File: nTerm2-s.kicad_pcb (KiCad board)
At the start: 2 copper layers, 147.3 x 55.9 mm, 108 parts, among them J1 VGA, J2 Keyboard, J3 Mouse, J4 Line-out/Speaker, J5 RS-232 V.24, J6 USB_C_Receptacle_USB2.0_16P, J7 Line-out/Speaker, K1 IM41 3V, K2 IM41 3V, K3 IM41 3V, Q1 BC817, Q2 BC817, Q3 BC817, Q4 BC817, Q5 BC817, Q6 BC817, Q7 BC817, Q8 BC817, SW1 IO0, SW2 RESET, SW3 DEFAULTS, U1 ESP32-WROOM-32, U2 LM386, U3 MAX3232E, U4 CP2102N-Axx-xQFN28, U5 NCP1117-3.3_SOT223, U6 USBLC6-2SC6

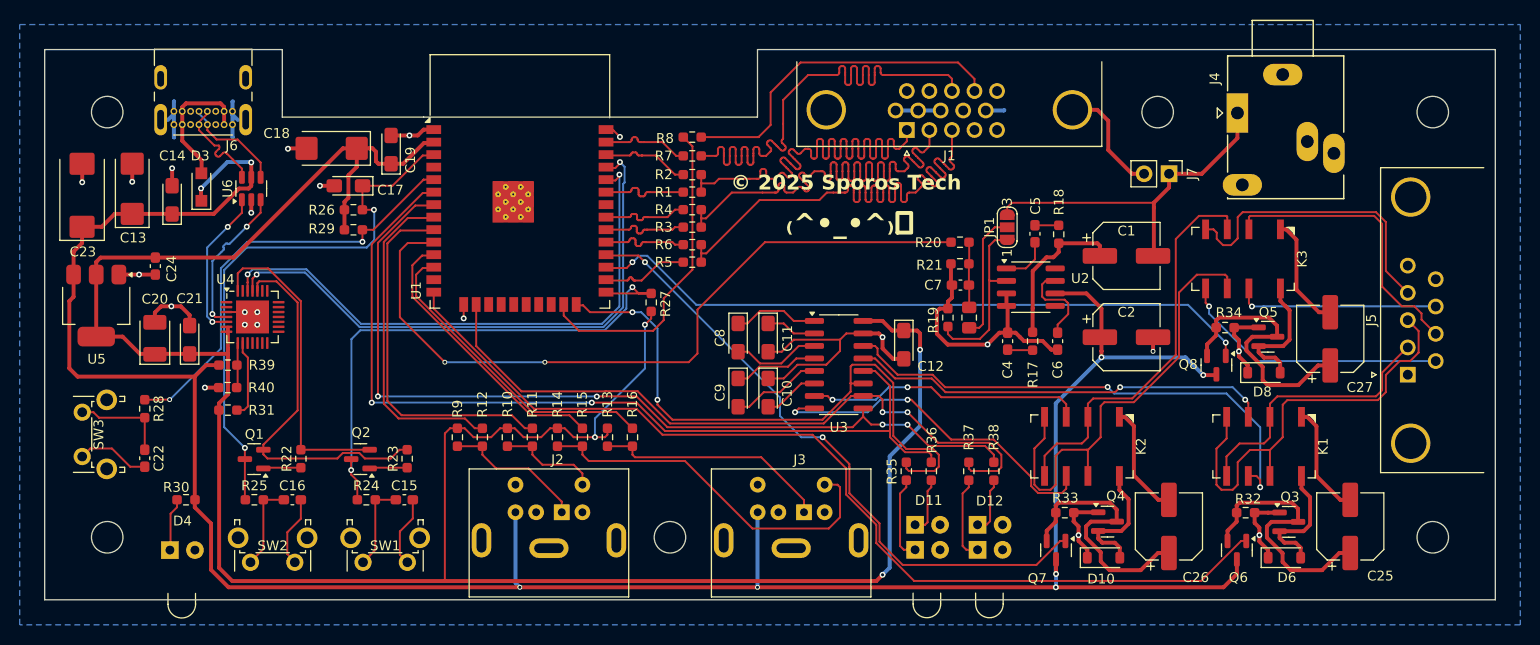
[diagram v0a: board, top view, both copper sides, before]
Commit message: Some small updates, a fix, and exported all libraries into the project, for distribution.
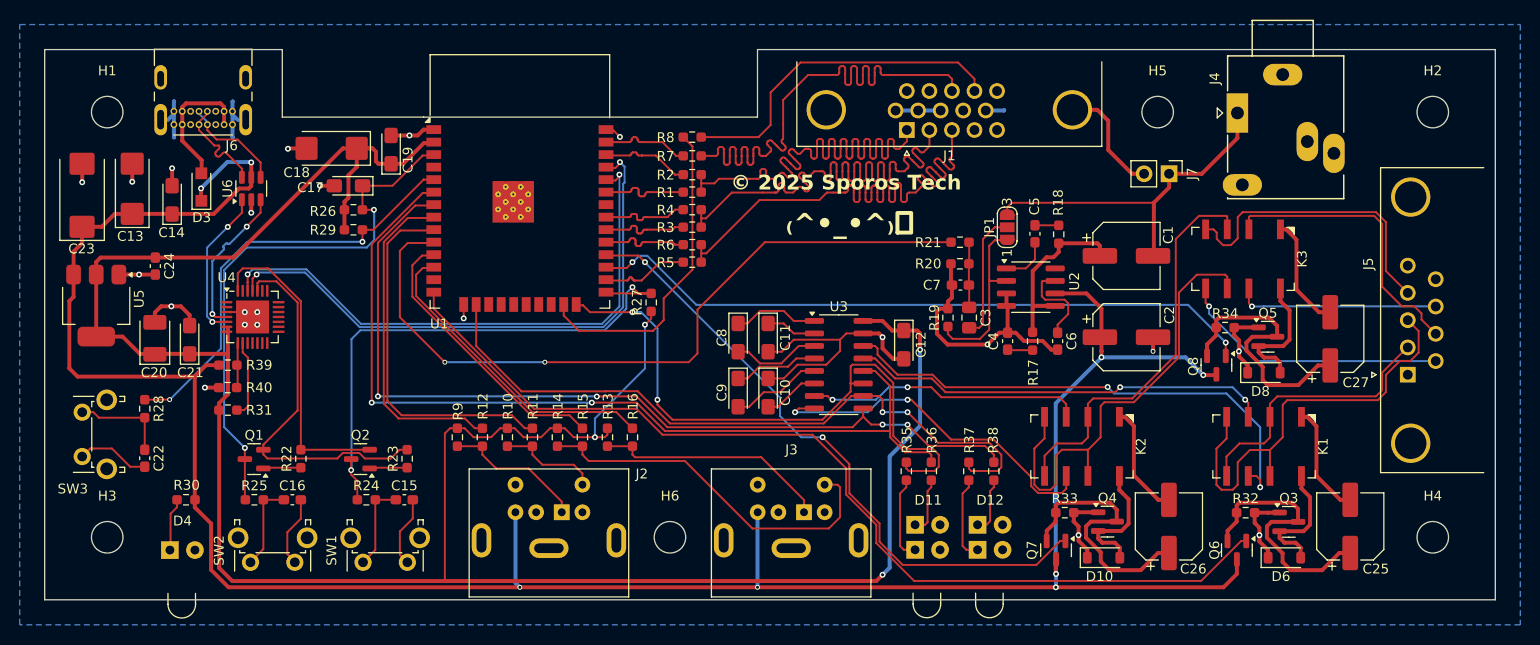
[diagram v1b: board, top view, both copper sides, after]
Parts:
- C1, C2, C25, C26, C27: footprint Capacitor_SMD:CP_Elec_6.3x7.7 -> CP_Elec_6.3x7.7
- C10, C11, C12, C14, C17, C19, C21, C8, C9: footprint Capacitor_Tantalum_SMD:CP_EIA-3216-18_Kemet-A_Pad1.58x1.35mm_HandSolder -> CP_EIA-3216-18_Kemet-A_Pad1.58x1.35mm_HandSolder
- C13, C18: footprint Capacitor_Tantalum_SMD:CP_EIA-6032-28_Kemet-C_Pad2.25x2.35mm_HandSolder -> CP_EIA-6032-28_Kemet-C_Pad2.25x2.35mm_HandSolder
- C15, C16, C22, C24, C4, C5, C6, C7: footprint Capacitor_SMD:C_0603_1608Metric_Pad1.08x0.95mm_HandSolder -> C_0603_1608Metric_Pad1.08x0.95mm_HandSolder
- C20: footprint Capacitor_Tantalum_SMD:CP_EIA-3528-21_Kemet-B_Pad1.50x2.35mm_HandSolder -> CP_EIA-3528-21_Kemet-B_Pad1.50x2.35mm_HandSolder
- C23: footprint Capacitor_Tantalum_SMD:CP_EIA-7343-30_AVX-N_Pad2.25x2.55mm_HandSolder -> CP_EIA-7343-30_AVX-N_Pad2.25x2.55mm_HandSolder
- C3: footprint Capacitor_SMD:C_0805_2012Metric_Pad1.18x1.45mm_HandSolder -> C_0805_2012Metric_Pad1.18x1.45mm_HandSolder
- D10, D6, D8: footprint Diode_SMD:D_SOD-123 -> D_SOD-123
- D11, D12: footprint Sporos_Tech_Footprints:DIALIGHT_LED_3MM_DOUBLE -> DIALIGHT_LED_3MM_DOUBLE
- D3: footprint Diode_SMD:Nexperia_CFP3_SOD-123W -> Nexperia_CFP3_SOD-123W
- D4: footprint Sporos_Tech_Footprints:DIALIGHT_LED_3MM_SINGLE -> DIALIGHT_LED_3MM_SINGLE
- H1, H2, H3, H4, H5, H6: footprint MountingHole:MountingHole_3.2mm_M3 -> MountingHole_3.2mm_M3
- J1: footprint Sporos_Tech_Footprints:DSUB-15-HD_Female_Horizontal_P2.29x1.98mm_EdgePinOffset3.03mm_Housed_MountingHolesOffset4.94mm -> DSUB-15-HD_Female_Horizontal_P2.29x1.98mm_EdgePinOffset3.03mm_Housed_MountingHolesOffset4.94mm
- J2, J3: footprint Custom_Footprints:Connector_Mini-DIN_Female_6Pin_2rows -> Connector_Mini-DIN_Female_6Pin_2rows
- J4: footprint Sporos_Tech_Footprints:Jack_3.5mm_Ledino_KB3SPRS_Horizontal-alt -> Jack_3.5mm_Ledino_KB3SPRS_Horizontal-alt
- J5: footprint Sporos_Tech_Footprints:DSUB-9_Male_Horizontal_P2.77x2.84mm_EdgePinOffset4.94mm_Housed_MountingHolesOffset7.48mm -> DSUB-9_Male_Horizontal_P2.77x2.84mm_EdgePinOffset4.94mm_Housed_MountingHolesOffset7.48mm
- J6: footprint Sporos_Tech_Footprints:USB_C_Receptacle_Molex_213716-0001 -> USB_C_Receptacle_Molex_213716-0001
- J7: footprint Connector_PinHeader_2.54mm:PinHeader_1x02_P2.54mm_Vertical -> PinHeader_1x02_P2.54mm_Vertical
- JP1: footprint Jumper:SolderJumper-3_P1.3mm_Open_RoundedPad1.0x1.5mm_NumberLabels -> SolderJumper-3_P1.3mm_Open_RoundedPad1.0x1.5mm_NumberLabels
- K1, K2, K3: footprint Sporos_Tech_Footprints:Relay_DPDT_AXICOM_IMSeries_Gullwing -> Relay_DPDT_AXICOM_IMSeries_Gullwing
- Q1, Q2, Q3, Q4, Q5, Q6, Q7, Q8: footprint Package_TO_SOT_SMD:SOT-23 -> SOT-23
- R1, R10, R11, R12, R13, R14, R15, R16, R17, R18, R19, R2, R20, R21, R22, R23, R24, R25, R26, R27, R28, R29, R3, R30, R31, R32, R33, R34, R35, R36, R37, R38, R39, R4, R40, R5, R6, R7, R8, R9: footprint Resistor_SMD:R_0603_1608Metric_Pad0.98x0.95mm_HandSolder -> R_0603_1608Metric_Pad0.98x0.95mm_HandSolder
- SW1, SW2, SW3: footprint Sporos_Tech_Footprints:SW_Tactile_SPST_Angled_PTS645Vx58-2LFS-alt -> SW_Tactile_SPST_Angled_PTS645Vx58-2LFS-alt
- U1: footprint RF_Module:ESP32-WROOM-32 -> ESP32-WROOM-32
- U2: footprint Package_SO:SOIC-8_3.9x4.9mm_P1.27mm -> SOIC-8_3.9x4.9mm_P1.27mm
- U3: footprint Package_SO:SOIC-16_3.9x9.9mm_P1.27mm -> SOIC-16_3.9x9.9mm_P1.27mm
- U4: footprint Sporos_Tech_Footprints:QFN-28-1EP_5x5mm_P0.5mm_EP3.35x3.35mm_handsolder -> QFN-28-1EP_5x5mm_P0.5mm_EP3.35x3.35mm_handsolder
- U5: footprint Package_TO_SOT_SMD:SOT-223-3_TabPin2 -> SOT-223-3_TabPin2
- U6: footprint Package_TO_SOT_SMD:SOT-23-6 -> SOT-23-6
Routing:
- net Net-(C1-Pad1): track 15.8 -> 18.1 mm
